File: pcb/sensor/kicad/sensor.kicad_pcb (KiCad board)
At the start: 2 copper layers, 38 x 86 mm, 16 parts, among them J1 43045-0600, U1 FDC1004DGSR, U2 TPS7A2433DBVR, U3 ESDS312DBVR

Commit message: Prepare filled planes and enforce KiCad routing guardrails
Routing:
- net GND: vias 0 -> 7
- added copper zone on B.Cu, net GND
- added copper zone on F.Cu, net GND

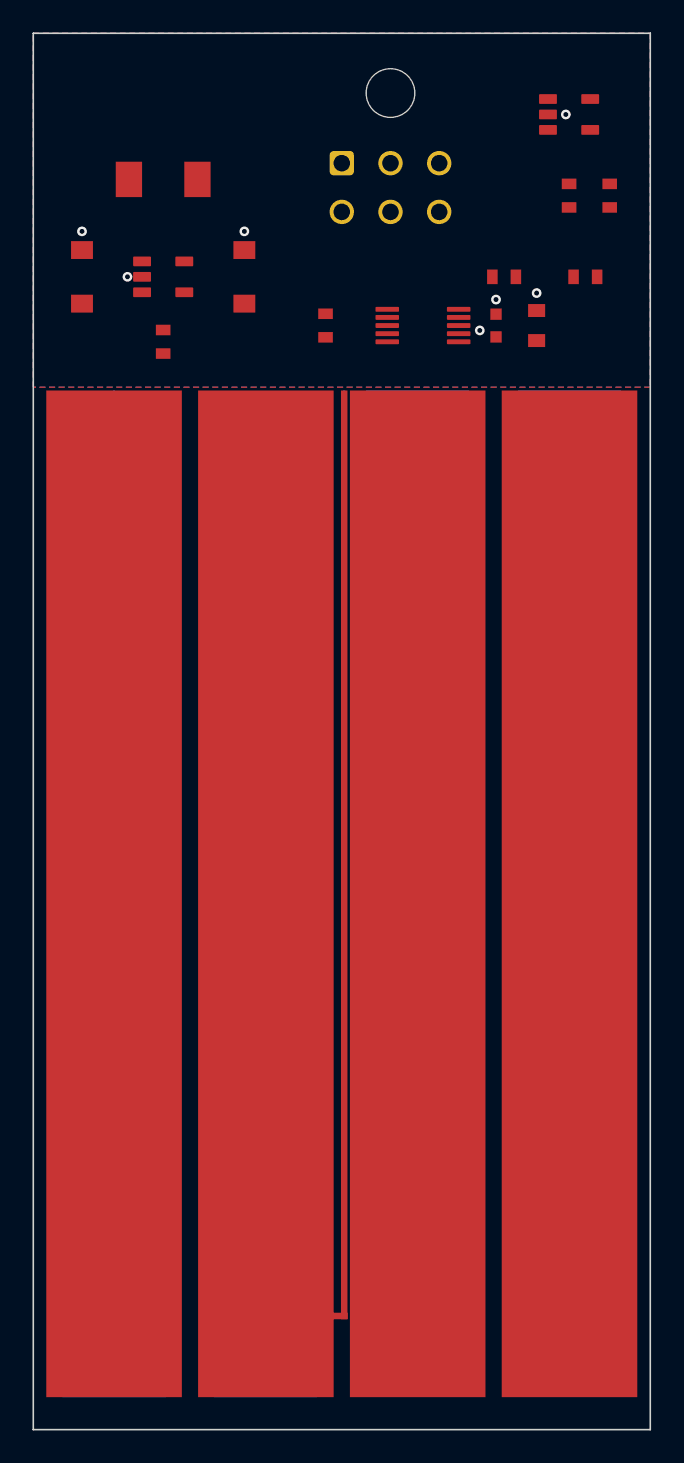
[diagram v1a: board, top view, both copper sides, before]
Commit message: Prepare compact three-board designs for owner routing
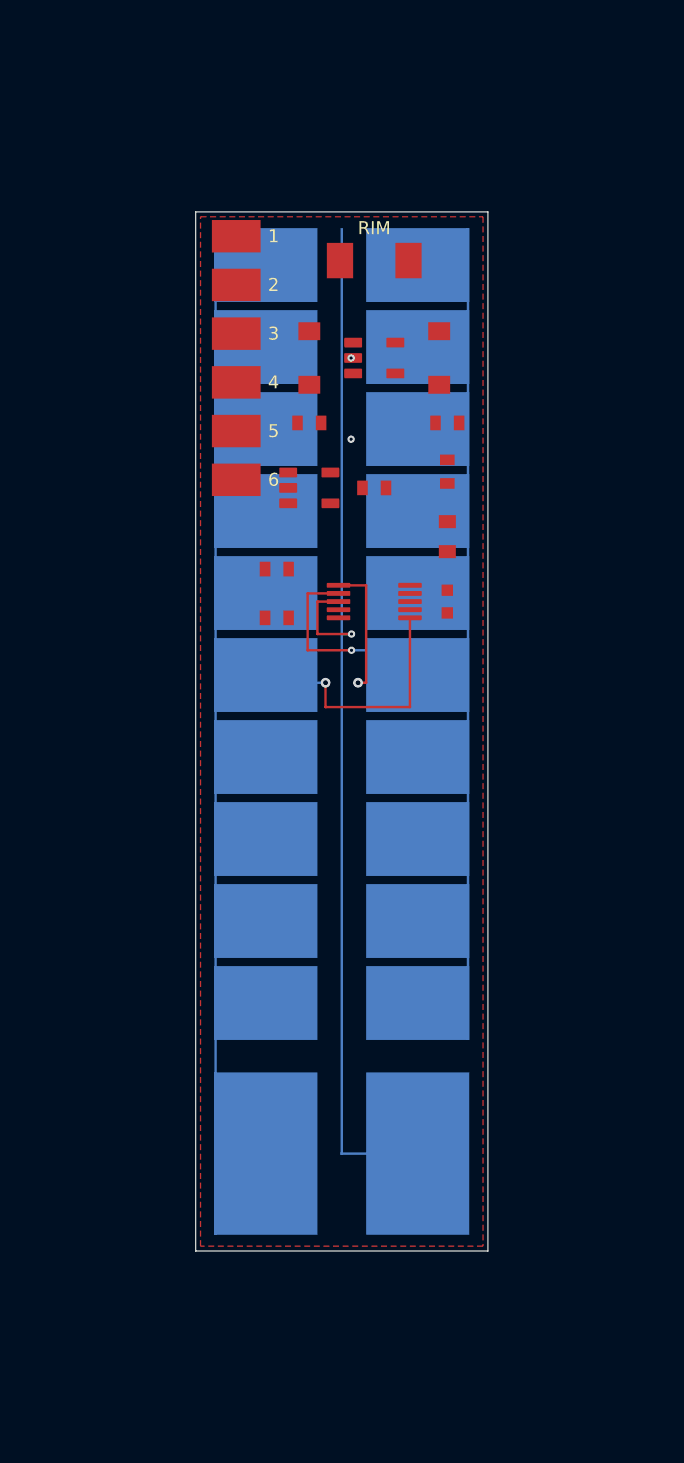
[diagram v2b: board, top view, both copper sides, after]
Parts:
- J1: value 43045-0600 -> PCB-SENSOR-PIGTAIL-6
- moved R2 33.1 mm to (96.0, 93.0), turned to 0 degrees
- moved R1 29.2 mm to (96.0, 90.0), turned to 0 degrees
- moved U3 28.0 mm to (98.0, 85.0)
- moved C3 17.3 mm to (106.5, 92.0)
- moved U1 17.3 mm to (102.0, 92.0)
- moved R3 15.3 mm to (102.0, 85.0)
- moved C1 14.9 mm to (98.0, 77.0)
- moved R4 14.7 mm to (106.5, 84.0), turned to 90 degrees
- moved C4 14.1 mm to (106.5, 88.0)
- moved D2 13.9 mm to (102.0, 71.0)
- moved U2 13.9 mm to (102.0, 77.0)
- moved J1 13.6 mm to (93.5, 77.0)
- moved C2 13.0 mm to (106.0, 77.0)
- moved R5 10.3 mm to (98.0, 81.0), turned to 0 degrees
- moved E1 10.0 mm to (100.0, 100.0)
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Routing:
- net SHLD2: track 0.00 -> 12.9 mm, vias 0 -> 1
- net CIN_LEVEL: track 0.00 -> 9.20 mm, vias 0 -> 1
- net SHLD1: track 0.00 -> 8.20 mm, vias 0 -> 1
- net CIN_RL: track 0.00 -> 6.00 mm, vias 0 -> 1
- net GND: vias 7 -> 2
- added copper zone on In1.Cu, net GND
- removed copper zone on B.Cu, net GND
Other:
- board size 38 x 86 mm -> 18 x 64 mm
- copper layers 2 -> 4
- board text added: "1"
- board text added: "2"
- board text added: "3"
- board text added: "4"
- board text added: "5"
- board text added: "6"
- board text added: "RIM"

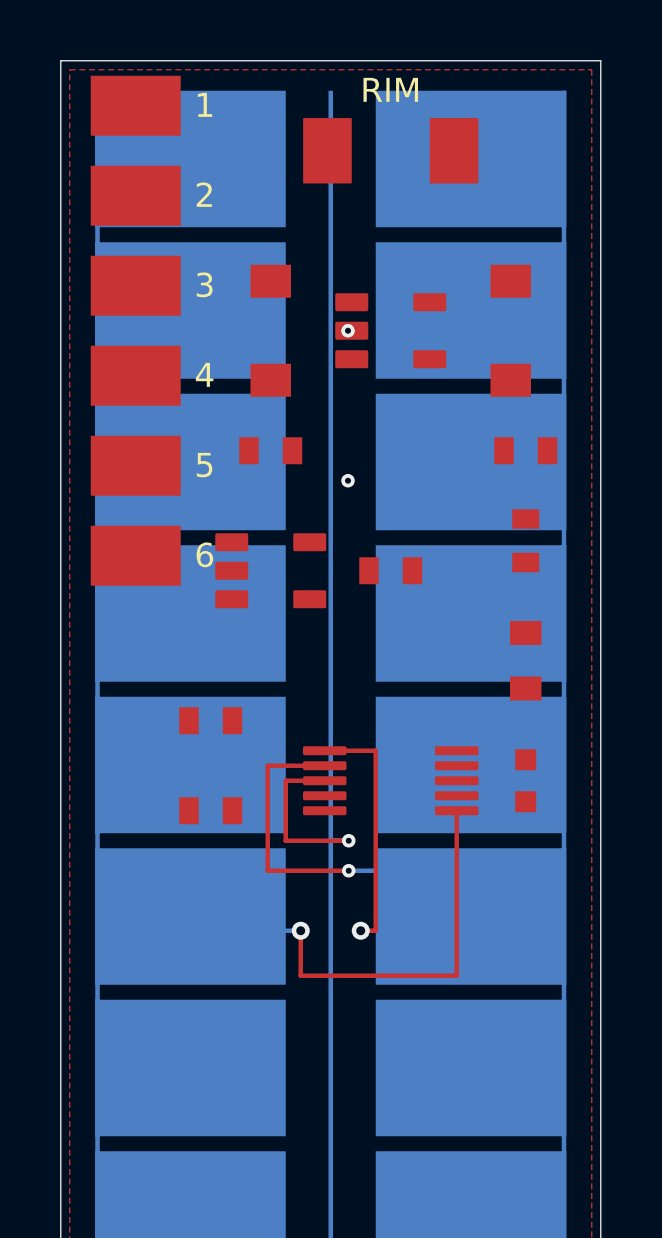
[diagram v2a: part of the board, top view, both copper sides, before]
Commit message: Accept completed sensor routing and preserve its checked baseline
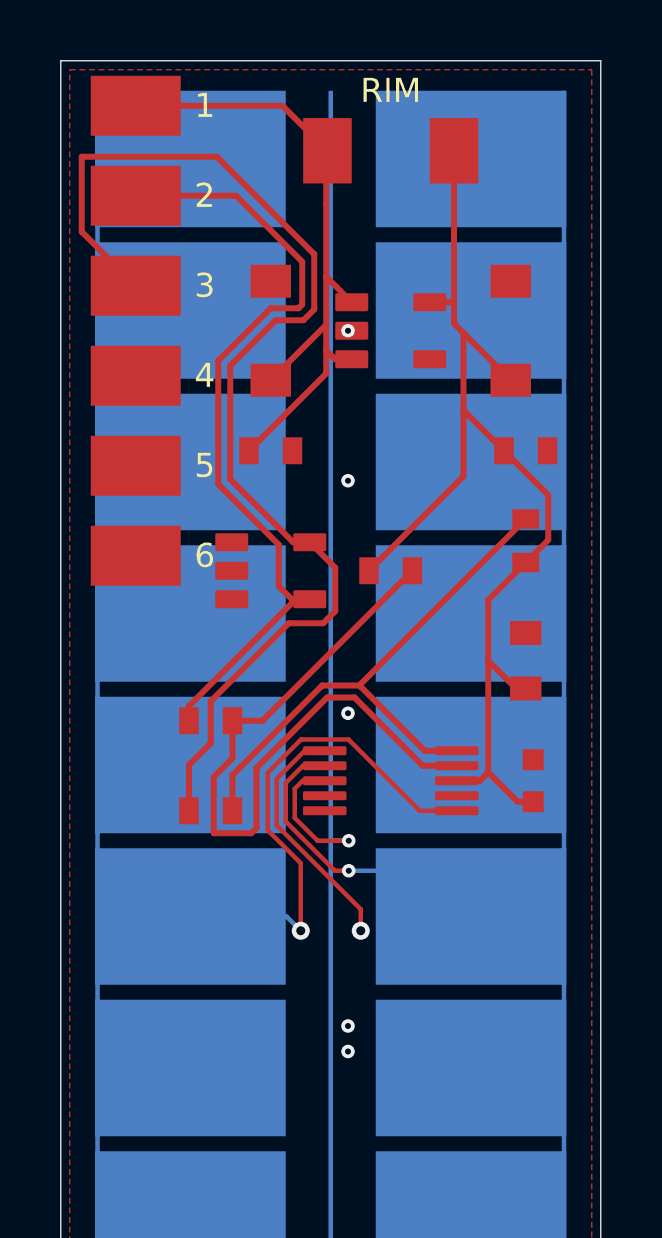
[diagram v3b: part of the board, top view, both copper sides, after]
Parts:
- moved C3 0.25 mm to (106.8, 92.0)
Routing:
- net SCL_CABLE: track 0.00 -> 38.9 mm
- net V3V3_SENSOR: track 0.00 -> 37.3 mm
- net SDA_CABLE: track 0.00 -> 27.0 mm
- net I2C_SDA: track 0.00 -> 24.2 mm
- net V5_SENSOR: track 0.00 -> 22.9 mm
- net I2C_SCL: track 0.00 -> 18.7 mm
- net SHLD2: track 12.9 -> 17.3 mm
- net CIN_RL: track 6.00 -> 4.80 mm
- net CIN_LEVEL: track 9.20 -> 10.3 mm
- net GND: vias 2 -> 5

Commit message: Prepare all three boards for standard JLCPCB ordering
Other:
- board text added: "CRYSTAL"
- board text added: "LEVEL SENSOR"
- board text added: "REV 1.0"
- board text added: "SHIM"
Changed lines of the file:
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@@
 		(at 98 81)
 		(property "Reference" "R5"
-			(at 0 -3 270)
-			(layer "F.SilkS")
-			(hide yes)
-			(effects
-				(font
-					(size 1.27 1.27)
+			(at 0 1.3 0)
+			(layer "F.SilkS")
+			(effects
+				(font
+					(size 0.8 0.8)
 					(thickness 0.15)
 				)
@@
 		(at 93.5 77)
 		(property "Reference" "J1"
-			(at 0 -3 0)
-			(layer "F.SilkS")
-			(hide yes)
-			(effects
-				(font
-					(size 1.27 1.27)
+			(at 0 9.5 0)
+			(layer "F.SilkS")
+			(effects
+				(font
+					(size 0.8 0.8)
 					(thickness 0.15)
 				)
@@
 		(at 106.5 88 90)
 		(property "Reference" "C4"
-			(at 0 -3 0)
-			(layer "F.SilkS")
-			(hide yes)
-			(effects
-				(font
-					(size 1.27 1.27)
+			(at 0 1.5 90)
+			(layer "F.SilkS")
+			(effects
+				(font
+					(size 0.8 0.8)
 					(thickness 0.15)
 				)
@@
 		(at 106.5 81)
 		(property "Reference" "R6"
-			(at 0 -3 270)
-			(layer "F.SilkS")
-			(hide yes)
-			(effects
-				(font
-					(size 1.27 1.27)
+			(at 0 1.1 0)
+			(layer "F.SilkS")
+			(effects
+				(font
+					(size 0.8 0.8)
 					(thickness 0.15)
 				)
@@
 		(at 106.75 92 90)
 		(property "Reference" "C3"
-			(at 0 -3 0)
-			(layer "F.SilkS")
-			(hide yes)
-			(effects
-				(font
-					(size 1.27 1.27)
+			(at -2.2 0 0)
+			(layer "F.SilkS")
+			(effects
+				(font
+					(size 0.8 0.8)
 					(thickness 0.15)
 				)
@@
 		(at 102 71)
 		(property "Reference" "D2"
-			(at 0 -3 0)
-			(layer "F.SilkS")
-			(hide yes)
-			(effects
-				(font
-					(size 1.27 1.27)
+			(at 0 2.5 0)
+			(layer "F.SilkS")
+			(effects
+				(font
+					(size 0.8 0.8)
 					(thickness 0.15)
 				)
@@
 		(at 98 77 90)
 		(property "Reference" "C1"
-			(at 0 -3 0)
-			(layer "F.SilkS")
-			(hide yes)
-			(effects
-				(font
-					(size 1.27 1.27)
+			(at 0 1.35 90)
+			(layer "F.SilkS")
+			(effects
+				(font
+					(size 0.8 0.8)
 					(thickness 0.15)
 				)
@@
 			(at 0 -3 0)
 			(layer "F.SilkS")
-			(hide yes)
-			(effects
-				(font
-					(size 1.27 1.27)
+			(effects
+				(font
+					(size 0.8 0.8)
 					(thickness 0.15)
 				)
@@
 		(at 106.5 84 90)
 		(property "Reference" "R4"
-			(at 0 -3 90)
-			(layer "F.SilkS")
-			(hide yes)
-			(effects
-				(font
-					(size 1.27 1.27)
+			(at 0 1.5 90)
+			(layer "F.SilkS")
+			(effects
+				(font
+					(size 0.8 0.8)
 					(thickness 0.15)
 				)
@@
 		(at 96 90)
 		(property "Reference" "R1"
-			(at 0 -3 270)
-			(layer "F.SilkS")
-			(hide yes)
-			(effects
-				(font
-					(size 1.27 1.27)
+			(at -2 0 90)
+			(layer "F.SilkS")
+			(effects
+				(font
+					(size 0.8 0.8)
 					(thickness 0.15)
 				)
@@
 		(at 102 85)
 		(property "Reference" "R3"
-			(at 0 -3 0)
-			(layer "F.SilkS")
-			(hide yes)
-			(effects
-				(font
-					(size 1.27 1.27)
+			(at 0 1.3 0)
+			(layer "F.SilkS")
+			(effects
+				(font
+					(size 0.8 0.8)
 					(thickness 0.15)
 				)
@@
 		(at 96 93)
 		(property "Reference" "R2"
-			(at 0 -3 270)
-			(layer "F.SilkS")
-			(hide yes)
-			(effects
-				(font
-					(size 1.27 1.27)
+			(at -2 0 90)
+			(layer "F.SilkS")
+			(effects
+				(font
+					(size 0.8 0.8)
 					(thickness 0.15)
 				)
@@
 		(at 102 77)
 		(property "Reference" "U2"
-			(at 0 -3 0)
-			(layer "F.SilkS")
-			(hide yes)
-			(effects
-				(font
-					(size 1.27 1.27)
+			(at 0 2.6 0)
+			(layer "F.SilkS")
+			(effects
+				(font
+					(size 0.8 0.8)
 					(thickness 0.15)
 				)
@@
 		(at 106 77 90)
 		(property "Reference" "C2"
-			(at 0 -3 0)
-			(layer "F.SilkS")
-			(hide yes)
-			(effects
-				(font
-					(size 1.27 1.27)
+			(at 0 1.8 90)
+			(layer "F.SilkS")
+			(effects
+				(font
+					(size 0.8 0.8)
 					(thickness 0.15)
 				)
@@
 		(at 98 85)
 		(property "Reference" "U3"
-			(at 0 -3 0)
-			(layer "F.SilkS")
-			(hide yes)
-			(effects
-				(font
-					(size 1.27 1.27)
+			(at 0 2.6 0)
+			(layer "F.SilkS")
+			(effects
+				(font
+					(size 0.8 0.8)
 					(thickness 0.15)
 				)
@@
 		(at 100 100)
 		(property "Reference" "E1"
-			(at 0 -3 0)
-			(layer "F.SilkS")
-			(hide yes)
-			(effects
-				(font
-					(size 1.27 1.27)
+			(at 0 30 0)
+			(layer "F.SilkS")
+			(effects
+				(font
+					(size 0.8 0.8)
 					(thickness 0.15)
 				)
@@
 		)
 		(embedded_fonts no)
+	)
+	(gr_line
+		(start 94 118.5)
+		(end 106 118.5)
+		(stroke
+			(width 0.15)
+			(type default)
+		)
+		(layer "F.SilkS")
+	)
+	(gr_line
+		(start 97 107)
+		(end 100 104)
+		(stroke
+			(width 0.15)
+			(type default)
+		)
+		(layer "F.SilkS")
+	)
+	(gr_line
+		(start 97.9 106.9)
+		(end 100 107.35)
+		(stroke
+			(width 0.15)
+			(type default)
+		)
+		(layer "F.SilkS")
+	)
+	(gr_line
+		(start 98.65 108)
+		(end 100 108.3)
+		(stroke
+			(width 0.15)
+			(type default)
+		)
+		(layer "F.SilkS")
+	)
+	(gr_line
+		(start 100 104)
+		(end 103 107)
+		(stroke
+			(width 0.15)
+			(type default)
+		)
+		(layer "F.SilkS")
+	)
+	(gr_line
+		(start 100 107.35)
+		(end 102.1 106.9)
+		(stroke
+			(width 0.15)
+			(type default)
+		)
+		(layer "F.SilkS")
+	)
+	(gr_line
+		(start 100 108.3)
+		(end 101.35 108)
+		(stroke
+			(width 0.15)
+			(type default)
+		)
+		(layer "F.SilkS")
+	)
+	(gr_line
+		(start 100 110)
+		(end 97 107)
+		(stroke
+			(width 0.15)
+			(type default)
+		)
+		(layer "F.SilkS")
+	)
+	(gr_line
+		(start 103 107)
+		(end 100 110)
+		(stroke
+			(width 0.15)
+			(type default)
+		)
+		(layer "F.SilkS")
 	)
 	(gr_line
@@
 		)
 	)
+	(gr_text "REV 1.0"
+		(at 100 123.2 0)
+		(layer "F.SilkS")
+		(effects
+			(font
+				(size 0.8 0.8)
+				(thickness 0.15)
+			)
+		)
+	)
 	(gr_text "RIM"
 		(at 102 69 0)
@@
 				(thickness 0.15)
 			)
+		)
+	)
+	(gr_text "LEVEL SENSOR"
+		(at 100 121 0)
+		(layer "F.SilkS")
+		(effects
+			(font
+				(size 1 1)
+				(thickness 0.15)
+			)
+		)
+	)
+	(gr_text "CRYSTAL"
+		(at 100 114 0)
+		(layer "F.SilkS")
+		(effects
+			(font
+				(size 1.2 1.2)
+				(thickness 0.15)
+			)
+		)
+	)
+	(gr_text "SHIM"
+		(at 100 116.3 0)
+		(layer "F.SilkS")
+		(effects
+			(font
+				(size 1.2 1.2)
+				(thickness 0.15)
+			)
